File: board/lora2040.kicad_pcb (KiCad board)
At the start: 4 copper layers, 22.4 x 31.1 mm, 66 parts, among them J1 u.FL, J16 Conn_01x01, J2 USB_B_Micro, U1 SX1262IMLTRT, U2 BGS12WN6E6327, U3 0900FM15K0039, U4 MR20H40 or AS3004204, U5 RP2040, U6 RTX-2016BD32-S-32.000-TR, U7 TPS73633DBV, Y2 ABM8-272-T3

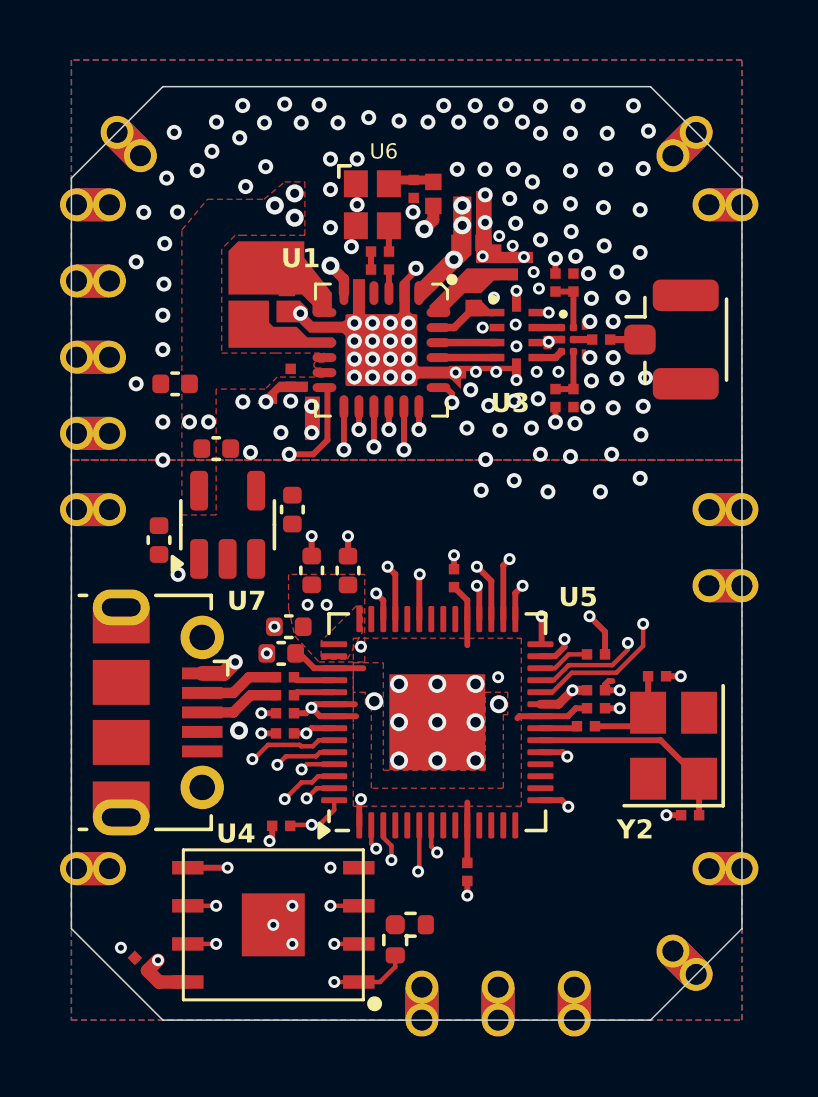
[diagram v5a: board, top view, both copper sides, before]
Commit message: BOM clean up and routing
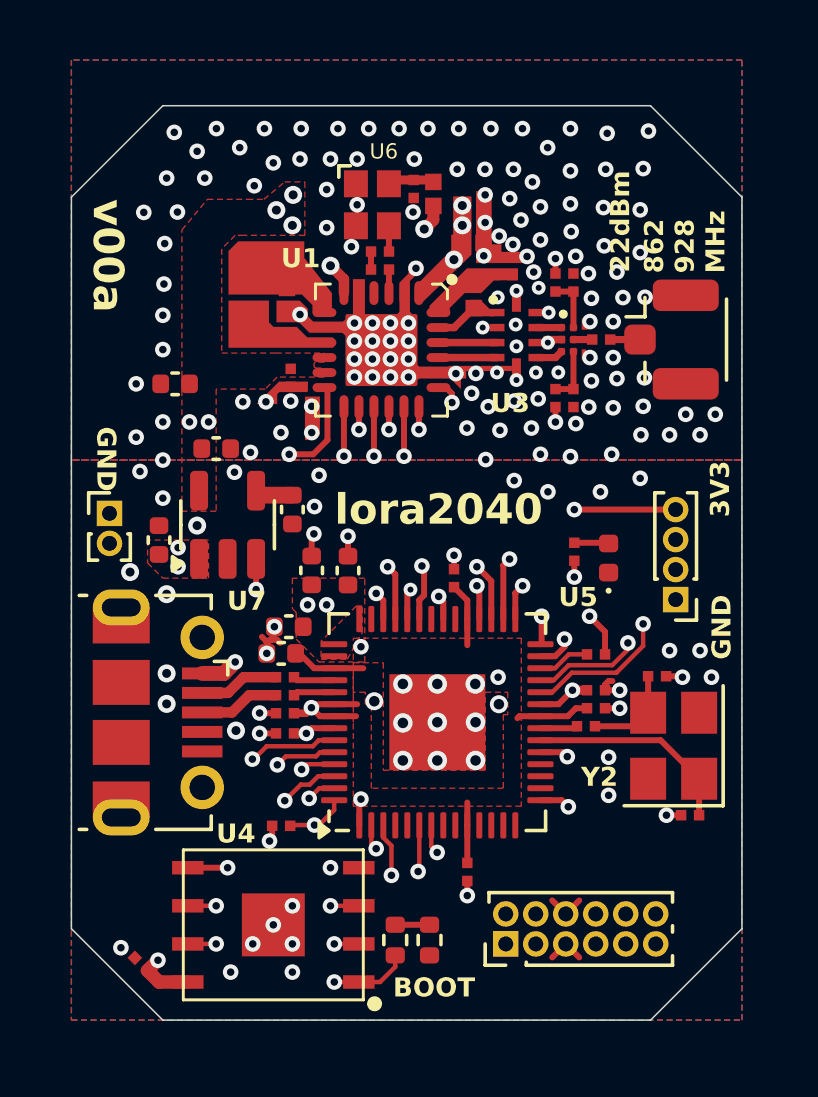
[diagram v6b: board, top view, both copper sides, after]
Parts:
- removed J16 (x16): Conn_01x01, custom-footprints:castellated_07mm
- added D1: LED, LED_SMD:LED_0402_1005Metric, F.Cu at (150.6, 96.5)
- added J5: Conn_01x02, Connector_PinHeader_1.00mm:PinHeader_1x02_P1.00mm_Vertical, F.Cu at (134.0, 95.0)
- added J6: Conn_02x06_Odd_Even, Connector_PinHeader_1.00mm:PinHeader_2x06_P1.00mm_Vertical, F.Cu at (147.2, 109.3)
- added J8: Conn_01x04, Connector_PinHeader_1.00mm:PinHeader_1x04_P1.00mm_Vertical, F.Cu at (152.9, 97.9)
- added R11: 1K, custom-footprints:sx126x_R_0201, F.Cu at (149.5, 96.3)
- moved R5 0.81 mm to (144.7, 109.2), turned to 90 degrees
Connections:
- net /VUSB renamed /VBUS
- U5 pad 24: unconnected-(U5-SWCLK-Pad24) -> /SWCLK
- U5 pad 25: unconnected-(U5-SWD-Pad25) -> /SWD
- U5 pad 35: unconnected-(U5-GPIO23-Pad35) -> /LED
- U5 pad 38: unconnected-(U5-GPIO26_ADC0-Pad38) -> /ADC0
- U5 pad 39: unconnected-(U5-GPIO27_ADC1-Pad39) -> /ADC1
- U5 pad 40: unconnected-(U5-GPIO28_ADC2-Pad40) -> /ADC2
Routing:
- net +3V3: track 50.6 -> 73.6 mm, vias 17 -> 18
- net /ADC1: track 0.00 -> 18.5 mm, vias 0 -> 1
- net /ADC2: track 0.00 -> 17.0 mm, vias 0 -> 1
- net /ADC0: track 0.00 -> 16.9 mm, vias 0 -> 1
- net unconnected-(U5-GPIO27_ADC1-Pad39): track 13.2 -> 0.00 mm, vias 1 -> 0
- net unconnected-(U5-GPIO28_ADC2-Pad40): track 11.6 -> 0.00 mm, vias 1 -> 0
- net /LED: track 0.00 -> 9.61 mm, vias 0 -> 2
- net /SWD: track 0.00 -> 8.13 mm, vias 0 -> 1
- net /SWCLK: track 0.00 -> 7.48 mm, vias 0 -> 1
- net unconnected-(U5-SWCLK-Pad24): track 4.80 -> 0.00 mm, vias 1 -> 0
- net /VBUS: track 5.62 -> 10.2 mm, vias 2 -> 4
- net GND: track 6.69 -> 11.2 mm, vias 171 -> 186
- net /UART0_TX: track 4.76 -> 9.25 mm
- net unconnected-(U5-SWD-Pad25): track 3.56 -> 0.00 mm, vias 1 -> 0
- net /SPI0_SCK: track 8.62 -> 11.7 mm
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- added copper zone on F.Cu, net /VBUS
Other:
- board size 22.4 x 31.1 mm -> 22.4 x 30.5 mm
- board text added: "22dBm"
- board text added: "3V3"
- board text added: "862 928 MHz"
- board text added: "BOOT"
- board text added: "GND"
- board text added: "lora2040"
- board text added: "v00a"

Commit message: v00a manufacturing files
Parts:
- L1: value 47nF -> 47nH
- moved J2 0.20 mm to (135.4, 101.6)
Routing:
- net GND: track 11.2 -> 13.9 mm, vias 186 -> 202
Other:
- board text removed: "Mitigate thermal effects on xtal"
